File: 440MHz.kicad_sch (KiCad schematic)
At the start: 50 parts, among them J5 BWSMA-KWE-Z001, U7 GRF5604, U9 SKYA21003

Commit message: More re-layout for the new design
Signed-off-by: Corey Minyard <corey@minyard.net>
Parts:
- C55: value 100pF -> 1nF
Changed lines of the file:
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@@
 			)
 		)
-		(property "Value" "100pF"
+		(property "Value" "1nF"
 			(at 103.124 136.906 90)
 			(effects

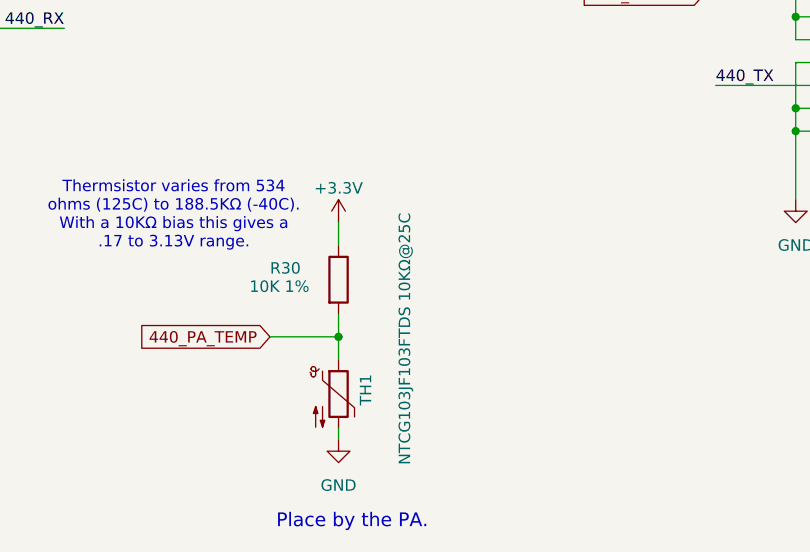
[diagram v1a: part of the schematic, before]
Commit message: Add some LEDs
Signed-off-by: Corey Minyard <corey@minyard.net>
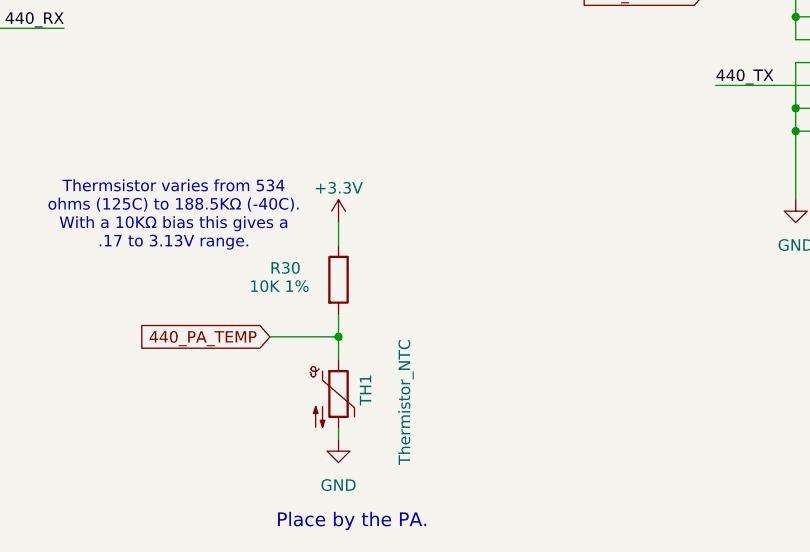
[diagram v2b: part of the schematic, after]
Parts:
- TH1: value NTCG103JF103FTDS 10KΩ@25C -> Thermistor_NTC
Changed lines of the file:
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@@
 			)
 		)
-		(property "Value" "NTCG103JF103FTDS 10KΩ@25C"
+		(property "Value" "Thermistor_NTC"
 			(at 149.606 181.864 90)
 			(effects
@@
 			)
 		)
-		(property "Datasheet" "NCU15XH103F60RC"
+		(property "Datasheet" "~"
 			(at 142.24 172.72 0)
 			(effects

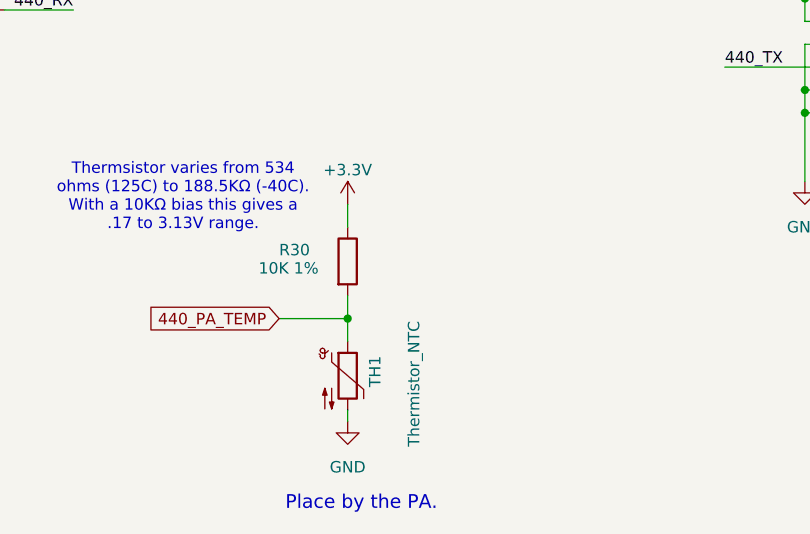
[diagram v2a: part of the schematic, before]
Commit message: Fix some components messed up by the previous change
Signed-off-by: Corey Minyard <corey@minyard.net>
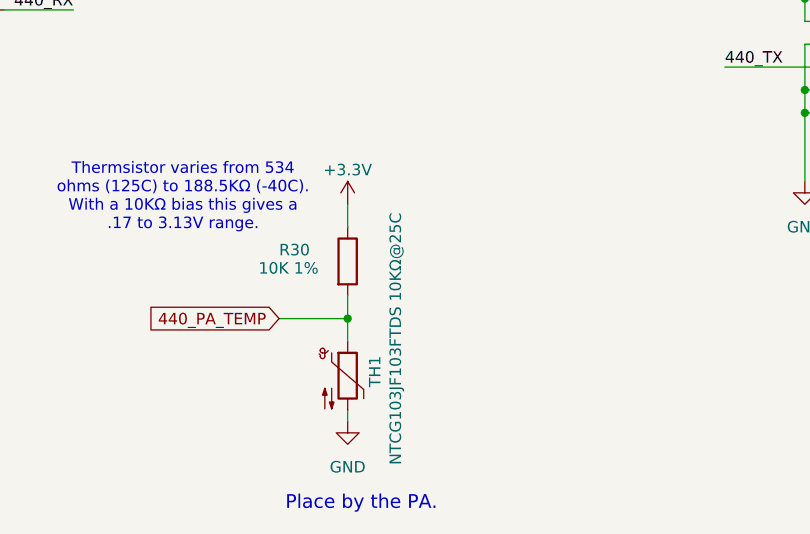
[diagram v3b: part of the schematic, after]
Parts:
- TH1: value Thermistor_NTC -> NTCG103JF103FTDS 10KΩ@25C
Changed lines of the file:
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@@
 			)
 		)
-		(property "Value" "Thermistor_NTC"
-			(at 149.606 181.864 90)
+		(property "Value" "NTCG103JF103FTDS 10KΩ@25C"
+			(at 147.574 183.896 90)
 			(effects
 				(font
